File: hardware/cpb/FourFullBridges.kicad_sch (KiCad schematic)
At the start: 31 parts, among them Q5 PMBT2222A, Q6 IRF9393, Q7 PMBT2222A, U7 SC18IS606, U8 KF33BDT, U9 MAX22200

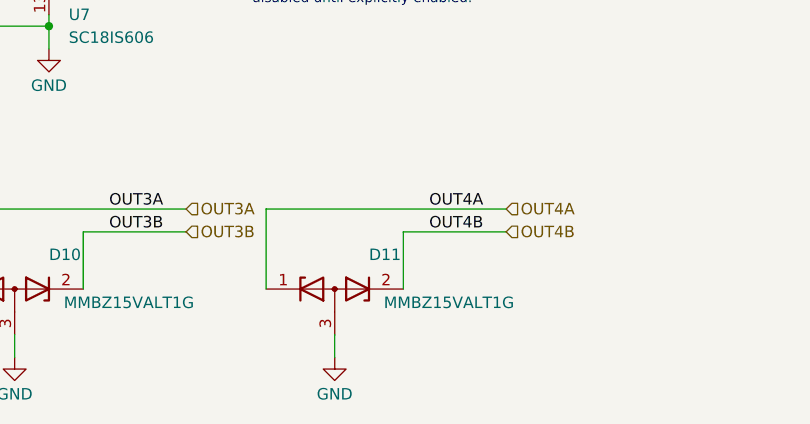
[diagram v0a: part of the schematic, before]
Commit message: cpb: routing in progress
- Adjust layout for easier routing.
- Pin swap clamping diodes to simplify routing.
- Route the high power nets
- Adjust plane pours.
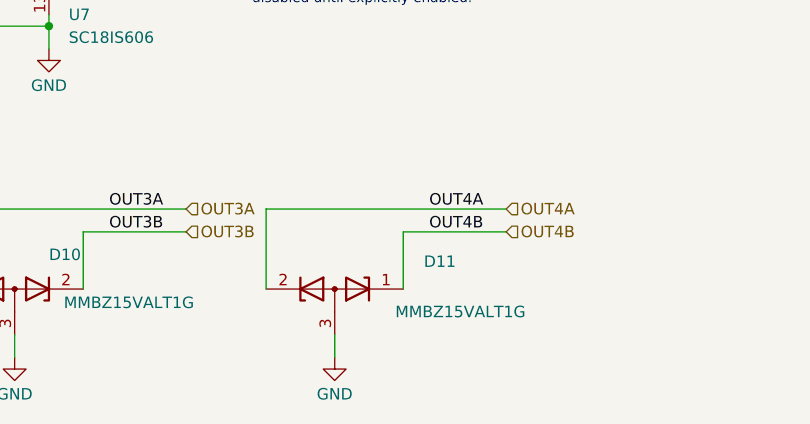
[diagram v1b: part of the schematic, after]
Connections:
- net OUT4A: now also D11.2 (K); no longer D11.1 (K)
- net OUT4B: now also D11.1 (K); no longer D11.2 (K)
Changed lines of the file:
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@@
 		(lib_id "Device:D_Zener_Dual_CommonAnode_KKA")
 		(at 130.81 187.96 0)
+		(mirror y)
 		(unit 1)
 		(exclude_from_sim no)
@@
 		(dnp no)
 		(property "Reference" "D11"
-			(at 136.398 184.15 0)
+			(at 142.494 184.912 0)
 			(effects
 				(font
@@
 		)
 		(property "Value" "MMBZ15VALT1G"
-			(at 143.51 189.484 0)
+			(at 144.78 190.5 0)
 			(effects
 				(font

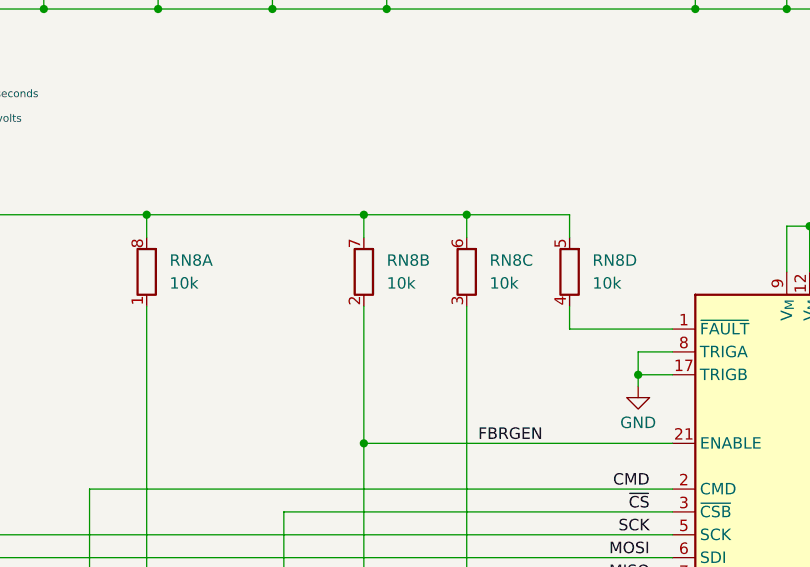
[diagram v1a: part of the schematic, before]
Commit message: cpb: Bill of materials updates
One layout change will result: some 1206 resistors became 2012.
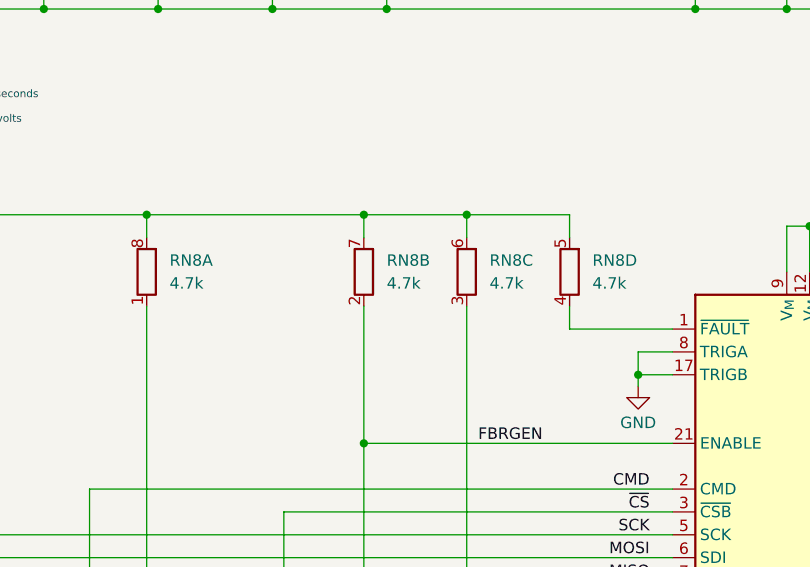
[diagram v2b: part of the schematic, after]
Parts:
- C36, C38: LCSC (none) -> C2178186
- C37, C39, C44: LCSC (none) -> C77047
- C40, C41, C42, C43, C45, C46, C47, C49: LCSC (none) -> C77055
- C48: LCSC (none) -> C29936
- C50: LCSC (none) -> C21122
- D10, D11, D8, D9: LCSC (none) -> C22582
- R47: footprint Resistor_SMD:R_1206_3216Metric -> Resistor_SMD:R_2010_5025Metric; LCSC (none) -> C2073579
- R49, R51: LCSC (none) -> C844918
- R54: LCSC (none) -> C844742
- RN8: value 10k -> 4.7k; LCSC (none) -> C327044
- RN9: LCSC (none) -> C327044
- U7: LCSC (none) -> C5190384
- U9: LCSC (none) -> C2845158
